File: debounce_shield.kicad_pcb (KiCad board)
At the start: 2 copper layers, 65 x 56 mm, 57 parts, among them J1 Conn_01x06, J2 RPi_GPIO, J3 Conn_01x06, J4 Conn_01x06, K1 CONN_3, P2 CONN_2, U1 74LVT04, U2 CAT24C32, U3 LTV-824, U4 LTV-824, U5 LTV-824

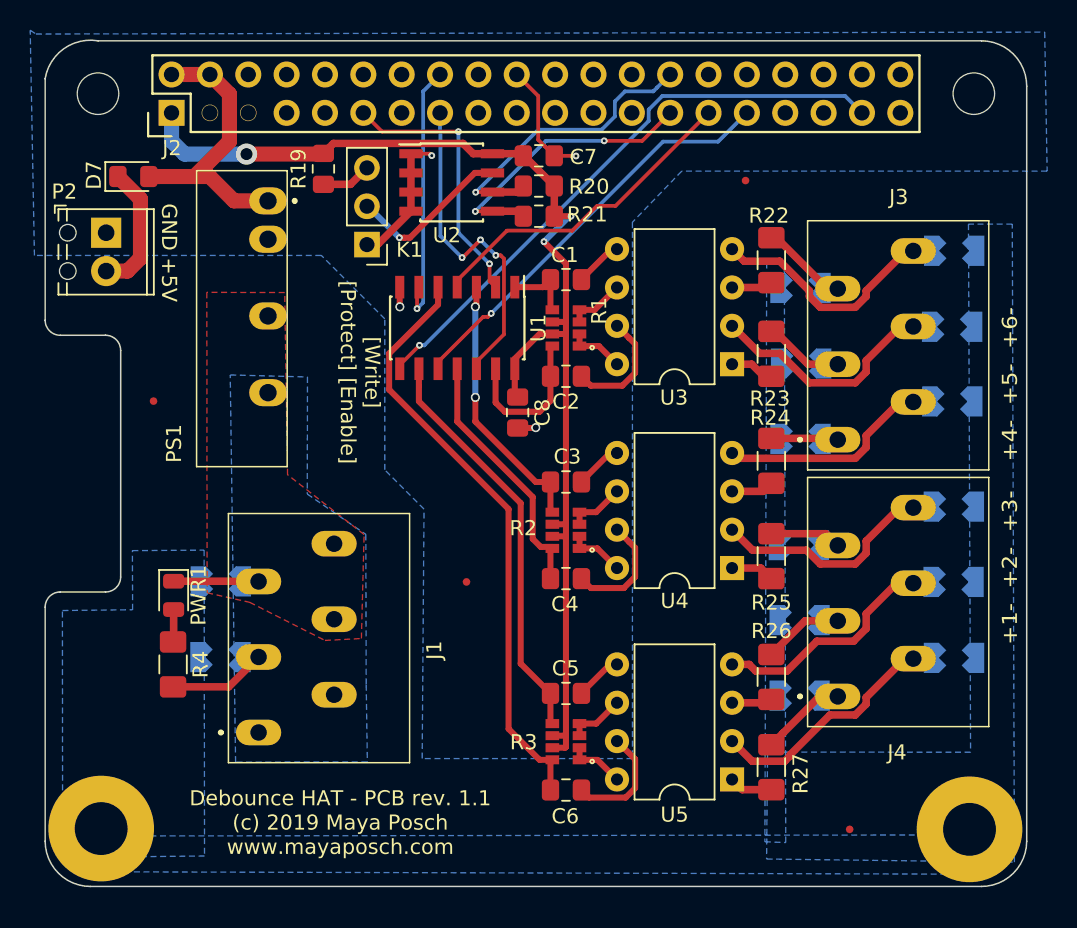
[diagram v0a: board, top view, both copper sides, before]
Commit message: Update v1.1 PCB layout. Update README.
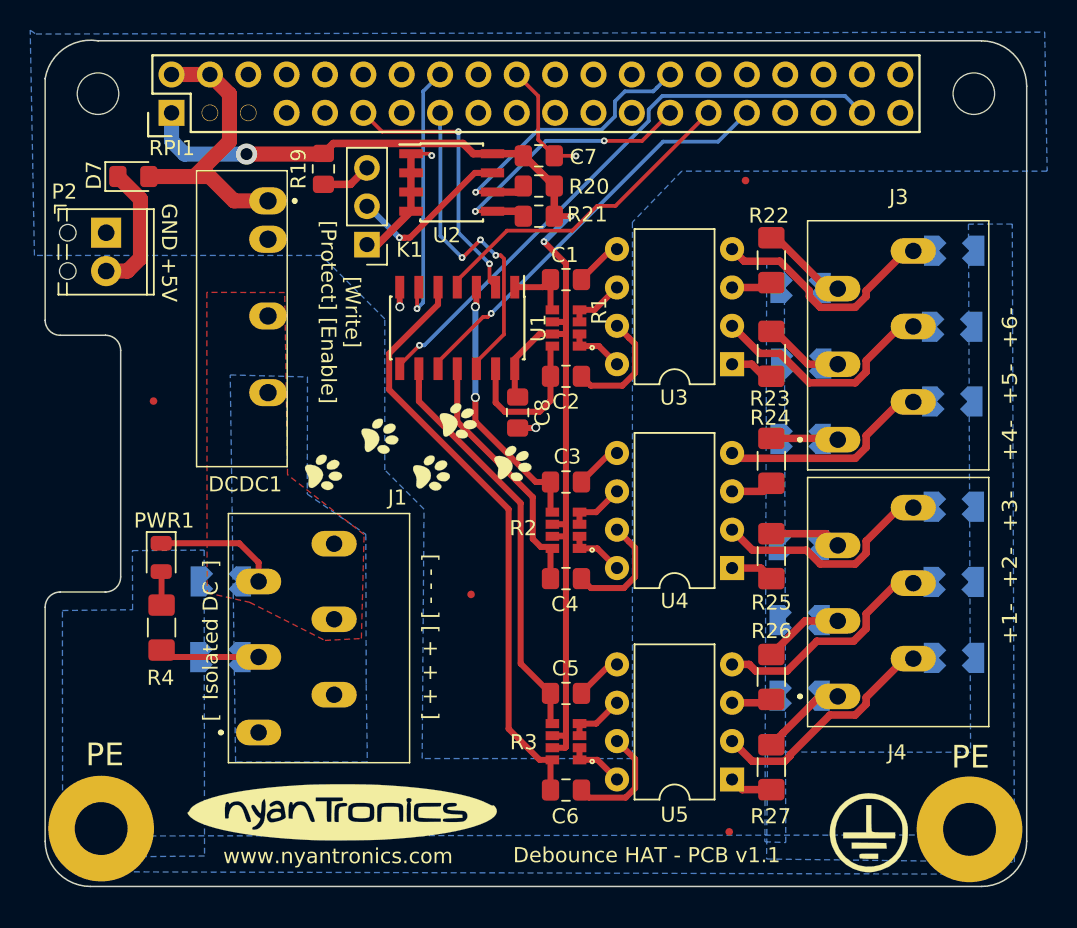
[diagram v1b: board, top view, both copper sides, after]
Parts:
- removed the REF** at (125.4, 108.4)
- removed the REF** at (150.8, 124.8)
- added ?: LOGO, kicad_art:kitten_paw_prints, F.Cu at (122.2, 100.9)
- added G***: LOGO, kicad_art:nyantronics_logo, F.Cu at (117.2, 123.6)
- added G***: LOGO, oshw:oshw, B.Cu at (129.6, 110.2)
- added G***: LOGO, kicad_art:earth_pe, F.Cu at (152.1, 125.0)
- added REF**: Fiducial_0.5mm_Dia_1mm_Outer, Fiducial:Fiducial_0.5mm_Dia_1mm_Outer, F.Cu at (125.7, 109.2)
- added REF**: Fiducial_0.5mm_Dia_1mm_Outer, Fiducial:Fiducial_0.5mm_Dia_1mm_Outer, F.Cu at (142.8, 125.0)
- moved PWR1 2.65 mm to (105.2, 106.8)
- moved R4 2.56 mm to (105.2, 111.4)
- renumbered PS1 to DCDC1, J2 to RPI1
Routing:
- net Net-(D1-Pad1): track 5.98 -> 8.58 mm
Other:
- board text added: "Debounce HAT - PCB v1.1"
- board text added: "PE"
- board text added: "[ + + + ] [ - - - ]"
- board text added: "[ Isolated DC ]"
- board text added: "www.nyantronics.com"
- board text removed: "Debounce HAT - PCB rev. 1.1 (c) 2019 Maya Posch www.mayaposch.com"

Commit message: Update schematic and PCB to revision 1.2
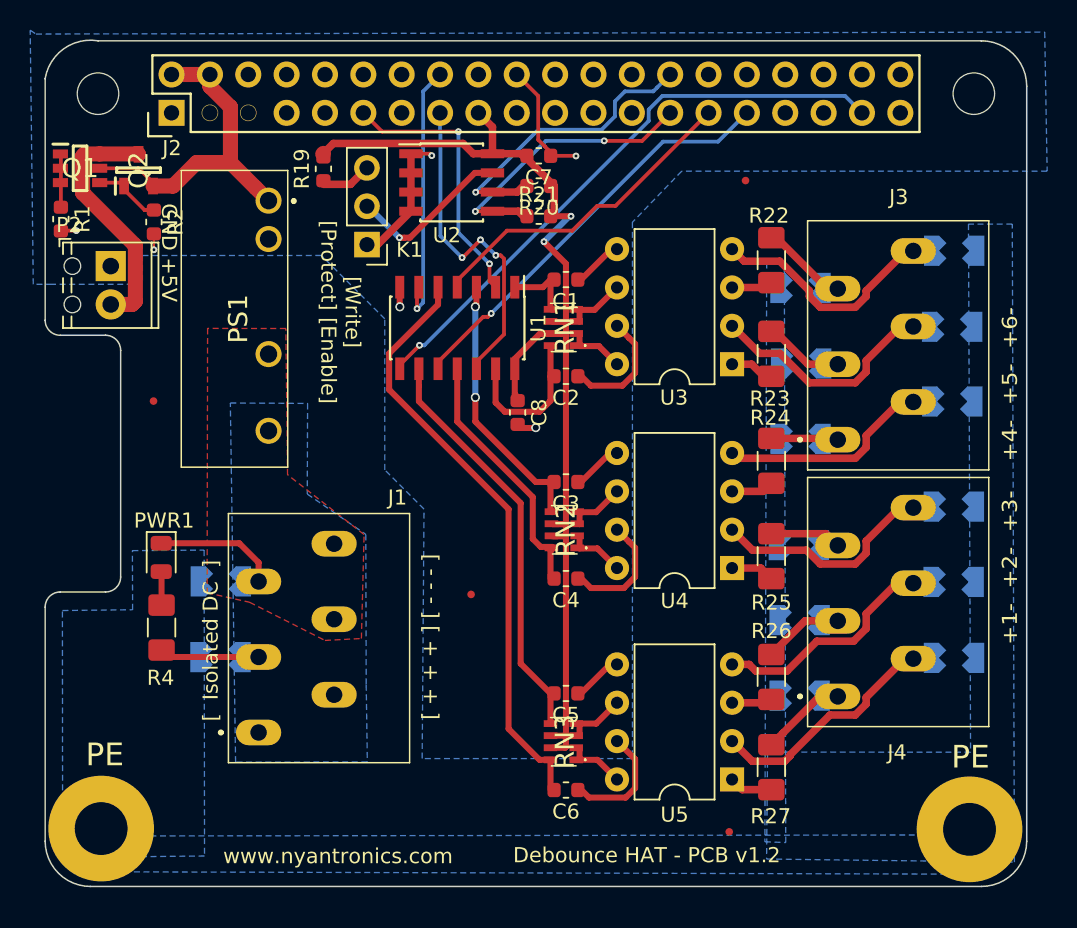
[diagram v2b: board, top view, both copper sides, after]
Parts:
- removed the ? at (122.2, 100.9)
- removed D7: DIODE, Diode_SMD:D_0805_2012Metric_Pad1.15x1.40mm_HandSolder
- removed DCDC1: REE-0505S, SamacSys_Parts:REE0505S
- removed G***: LOGO, kicad_art:nyantronics_logo
- removed G***: LOGO, oshw:oshw
- removed G***: LOGO, kicad_art:earth_pe
- removed R3: YC164-JR-0710KL, SamacSys_Parts:YC164
- added PS1: RFMM-0505S, RFMM-0505S:RFMM0505S, F.Cu at (110.3, 91.0)
- added Q1: DMMT5401-7, DMMT5401-7:SOT95P275X110-6N, F.Cu at (99.8, 81.0)
- added Q2: DMG2305UX-7, DMG2305UX-7:SOT96P240X100-3N, F.Cu at (103.7, 81.2)
- added RN1: YC164-JR-07100RL, YC164-JR-07100RL:YC164JR07220RL, F.Cu at (131.8, 91.6)
- added RN2: YC164-JR-07100RL, YC164-JR-07100RL:YC164JR07220RL, F.Cu at (131.9, 105.0)
- added RN3: YC164-JR-07100RL, YC164-JR-07100RL:YC164JR07220RL, F.Cu at (131.8, 119.0)
- C1, C2, C3, C4, C5, C6, C7, C8: footprint Capacitor_SMD:C_0805_2012Metric_Pad1.15x1.40mm_HandSolder -> Capacitor_SMD:C_0603_1608Metric
- R1: value YC164-JR-0710KL -> 10k 1%; footprint SamacSys_Parts:YC164 -> Resistor_SMD:R_0603_1608Metric
- R19, R20, R21: footprint Resistor_SMD:R_0805_2012Metric_Pad1.15x1.40mm_HandSolder -> Resistor_SMD:R_0603_1608Metric
- R2: value YC164-JR-0710KL -> 47k 1%; footprint SamacSys_Parts:YC164 -> Resistor_SMD:R_0603_1608Metric
- moved R1 34.2 mm to (98.6, 84.4), turned to 270 degrees
- moved R2 34.1 mm to (104.7, 84.6), turned to 270 degrees
- moved P2 2.23 mm to (101.9, 87.5)
- renumbered RPI1 to J2
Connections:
- J2 pad 1: +3.3V -> Net-(J2-Pad1)
- J2 pad 17: Net-(J2-Pad17) -> +3.3V
- J2 pad 25: Net-(J2-Pad25) -> GND
- R1 pad 1: Net-(R1-Pad1) -> Net-(Q1-Pad1)
- R1 pad 2: Net-(R1-Pad1) -> GND
- R2 pad 1: Net-(R2-Pad1) -> Net-(Q1-Pad4)
- R2 pad 2: Net-(R2-Pad1) -> GND
- U3 pad 6: Net-(R1-Pad3) -> Net-(RN1-Pad3)
- U3 pad 8: Net-(R1-Pad1) -> Net-(RN1-Pad1)
- U4 pad 6: Net-(R2-Pad3) -> Net-(RN2-Pad3)
- U4 pad 8: Net-(R2-Pad1) -> Net-(RN2-Pad1)
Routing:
- net +3.3V: track 79.9 -> 70.8 mm, vias 3 -> 2
- net /+5V_in: track 8.65 -> 16.5 mm
- net Net-(Q1-Pad4): track 0.00 -> 4.47 mm
- net Net-(RN1-Pad3): track 0.00 -> 3.89 mm
- net Net-(R1-Pad3): track 3.89 -> 0.00 mm
- net Net-(RN2-Pad3): track 0.00 -> 3.85 mm
- net Net-(R2-Pad3): track 3.85 -> 0.00 mm
- net Net-(RN2-Pad1): track 0.00 -> 3.82 mm
- net Net-(R2-Pad1): track 3.82 -> 0.00 mm
- net Net-(RN1-Pad1): track 0.00 -> 3.78 mm
- net Net-(R1-Pad1): track 3.78 -> 0.00 mm
- net Net-(Q1-Pad1): track 0.00 -> 3.58 mm
- net +5V: track 19.4 -> 22.4 mm
- net GND: track 52.1 -> 54.2 mm, vias 4 -> 6
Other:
- board text added: "Debounce HAT - PCB v1.2"
- board text removed: "Debounce HAT - PCB v1.1"

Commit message: Reduce WP header to two pins. Clean-up PCB layout. Re-add art.
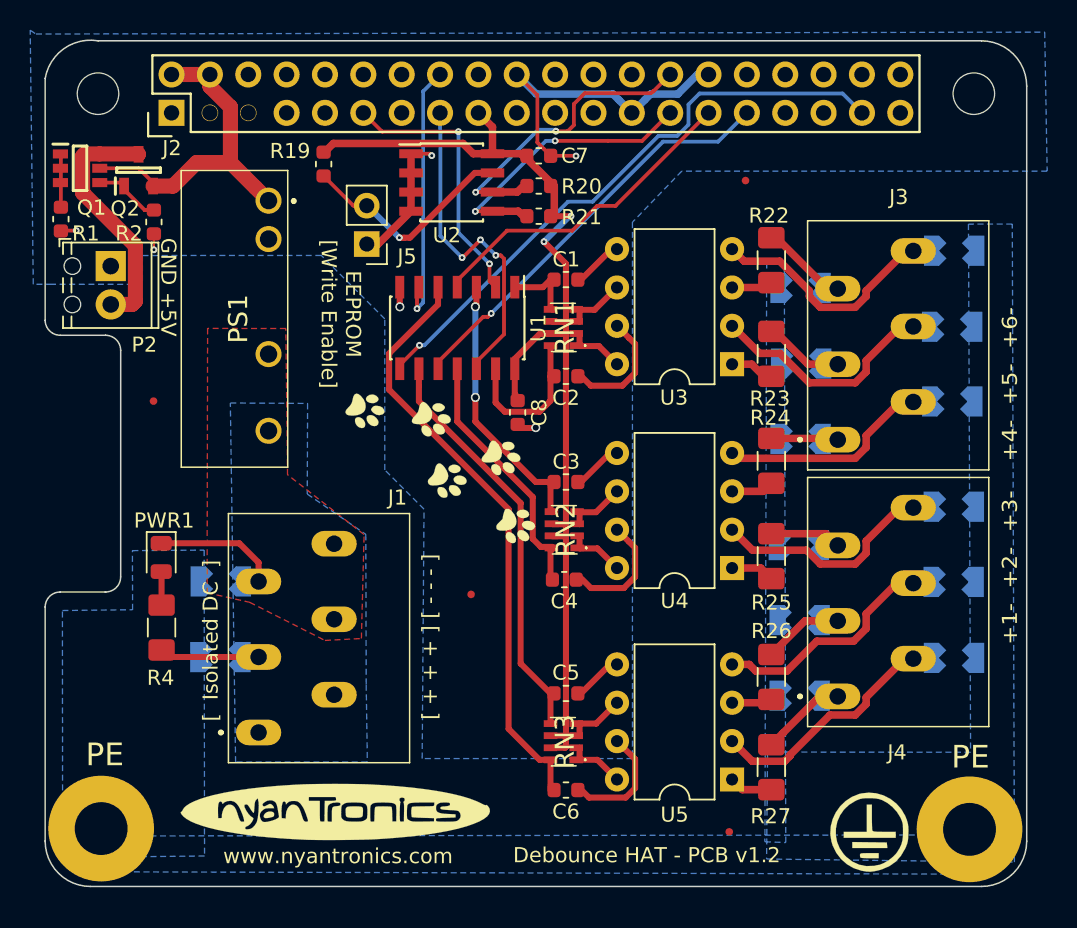
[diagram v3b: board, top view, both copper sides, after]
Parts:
- removed K1: CONN_3, Connector_PinHeader_2.54mm:PinHeader_1x03_P2.54mm_Vertical
- added G***: LOGO, oshw:oshw, B.Cu at (128.9, 110.7)
- added G***: LOGO, libs:earth_pe, F.Cu at (152.1, 125.0)
- added G***: LOGO, libs:kitten_paw_prints, F.Cu at (123.7, 100.9)
- added G***: LOGO, libs:nyantronics_logo, F.Cu at (116.7, 123.6)
- added J5: Conn_01x02, Connector_PinHeader_2.54mm:PinHeader_1x02_P2.54mm_Vertical, F.Cu at (118.8, 86.0)
- moved R19 0.32 mm to (116.0, 80.7), turned to 270 degrees
- moved C4 0.13 mm to (131.9, 108.3)
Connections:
- R19 pad 1: Net-(K1-Pad3) -> +3.3V
- R19 pad 2: +3.3V -> Net-(J5-Pad2)
- U2 pad 7: Net-(K1-Pad2) -> Net-(J5-Pad2)
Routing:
- net GND: track 54.2 -> 68.9 mm
- net Net-(J5-Pad2): track 0.00 -> 14.6 mm, vias 0 -> 1
- net Net-(K1-Pad2): track 11.0 -> 0.00 mm, vias 1 -> 0
- net Net-(K1-Pad3): track 3.33 -> 0.00 mm
- net IDSCL: track 20.0 -> 20.4 mm, vias 1 -> 2
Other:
- board text added: "EEPROM [Write Enable]"
- board text removed: "[Write] [Protect] [Enable]"

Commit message: Reduce spark gaps by 30%. DRC fixes.
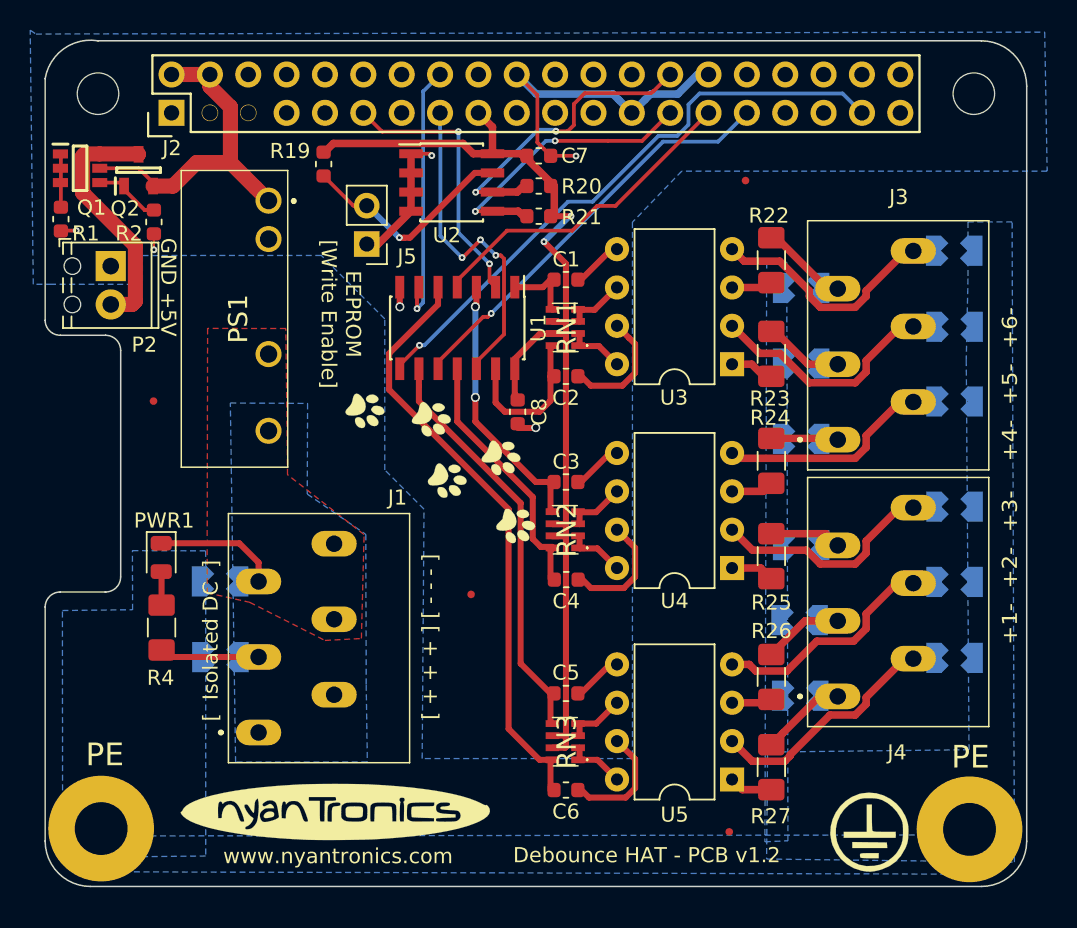
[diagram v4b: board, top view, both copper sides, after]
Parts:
- moved E5 0.16 mm to (157.7, 91.5)
- moved E10 0.15 mm to (147.6, 106.0)
- moved E7 0.15 mm to (157.7, 96.5)
- moved C4 0.13 mm to (132.0, 108.3)
- moved RN1 0.13 mm to (132.0, 91.6)
- moved RN3 0.13 mm to (132.0, 119.0)
- moved E11 0.06 mm to (157.7, 108.4)
- moved RN2 0.06 mm to (132.0, 105.0)
- moved E2 0.05 mm to (109.1, 108.4)

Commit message: Replace RFMM DC-DC with RKZE. Add EMC components.
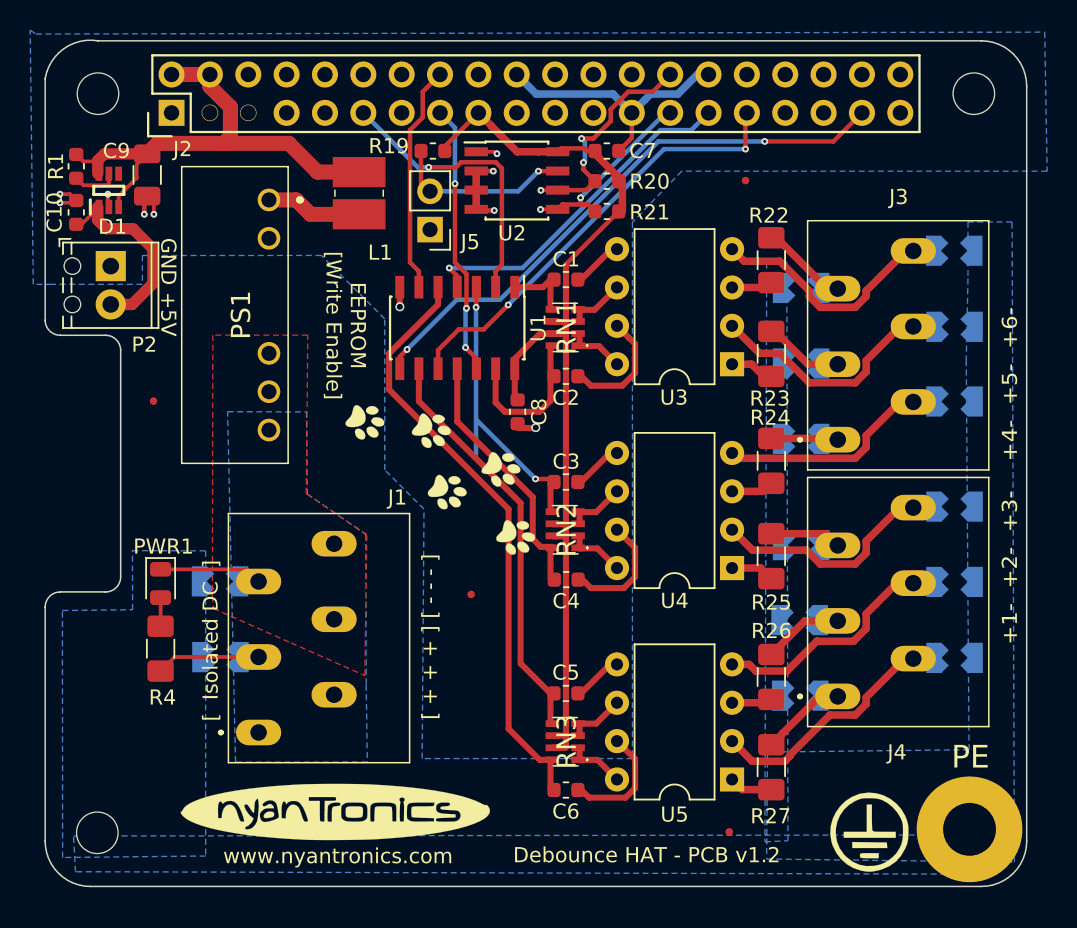
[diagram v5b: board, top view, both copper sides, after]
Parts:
- removed H2: MountingHole_Pad, MountingHole:MountingHole_3.5mm_Pad
- removed Q1: DMMT5401-7, DMMT5401-7:SOT95P275X110-6N
- removed Q2: DMG2305UX-7, DMG2305UX-7:SOT96P240X100-3N
- removed R2: 47k 1%, Resistor_SMD:R_0603_1608Metric
- added ?: , RPi_Hat:RPi_Hat_Mounting_Hole, F.Cu at (101.0, 125.0)
- added C10: 100 nF, Capacitor_SMD:C_0603_1608Metric, F.Cu at (99.6, 83.9)
- added C9: 10uF, Capacitor_SMD:C_1206_3216Metric, F.Cu at (104.3, 81.5)
- added D1: LM66100DCKR, LM66100DCKR:SOP65P210X110-6N, F.Cu at (101.7, 82.5)
- added L1: RLS-126, RLS-126:RLS126, F.Cu at (118.3, 82.7)
- PS1: value RFMM-0505S -> RKZE-0505S; footprint RFMM-0505S:RFMM0505S -> RKZE-0505S:RKZE0512SHP
- moved PS1 8.13 mm to (112.3, 83.1)
- moved R19 7.29 mm to (123.2, 79.9), turned to 180 degrees
- moved C7 4.52 mm to (134.7, 79.9)
- moved R20 4.52 mm to (134.7, 81.9)
- moved R21 4.52 mm to (134.7, 83.9)
- moved U2 4.32 mm to (128.8, 81.8)
- moved J5 4.30 mm to (123.0, 85.1)
- moved R1 3.64 mm to (99.6, 80.9)
- moved PWR1 1.73 mm to (105.2, 108.5)
- moved R4 1.40 mm to (105.2, 112.8), turned to 90 degrees
- moved G*** 0.76 mm to (123.7, 101.7)
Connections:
- PS1 pad 1: +5V -> Net-(L1-Pad2)
- R1 pad 1: Net-(Q1-Pad1) -> +5V
- R1 pad 2: GND -> Net-(D1-Pad5)
- R4 pad 1: Net-(PWR1-Pad2) -> Net-(E1-Pad2)
- R4 pad 2: Net-(E1-Pad2) -> Net-(PWR1-Pad2)
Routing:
- net +5V: track 22.4 -> 33.8 mm
- net Net-(L1-Pad2): track 0.00 -> 6.36 mm
- net IDSDA: track 18.9 -> 12.8 mm
- net +3.3V: track 70.7 -> 65.3 mm, vias 2 -> 0
- net IDSCL: track 20.4 -> 15.2 mm, vias 2 -> 3
- net Net-(Q1-Pad4): track 4.47 -> 0.00 mm
- net GND: track 68.9 -> 65.2 mm, vias 6 -> 10
- net Net-(Q1-Pad1): track 3.58 -> 0.00 mm
- net Net-(J2-Pad15): track 22.0 -> 18.4 mm
- net /+5V_in: track 16.5 -> 13.0 mm
- net Net-(D1-Pad5): track 0.00 -> 3.09 mm
- net Net-(J5-Pad2): track 14.6 -> 11.9 mm
- net Net-(C3-Pad2): track 17.6 -> 20.0 mm
- net Net-(J2-Pad16): track 17.6 -> 15.3 mm, vias 1 -> 0
- net Net-(J2-Pad31): track 27.7 -> 29.5 mm, vias 1 -> 2
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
